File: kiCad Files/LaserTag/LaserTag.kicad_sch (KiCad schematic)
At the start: 9 parts, among them J1 Conn_01x01_Male, J2 Conn_01x02_Male, U1 LM741

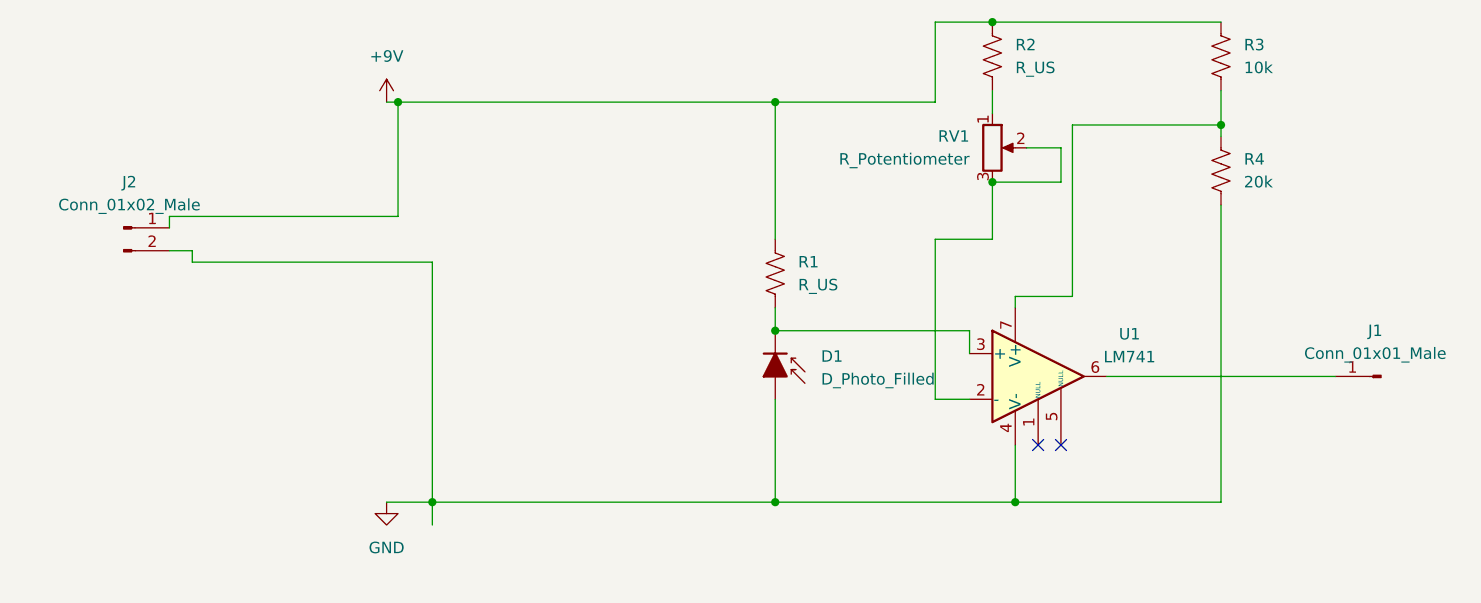
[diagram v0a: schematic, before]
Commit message: transmitter Circuit created + receiver resized
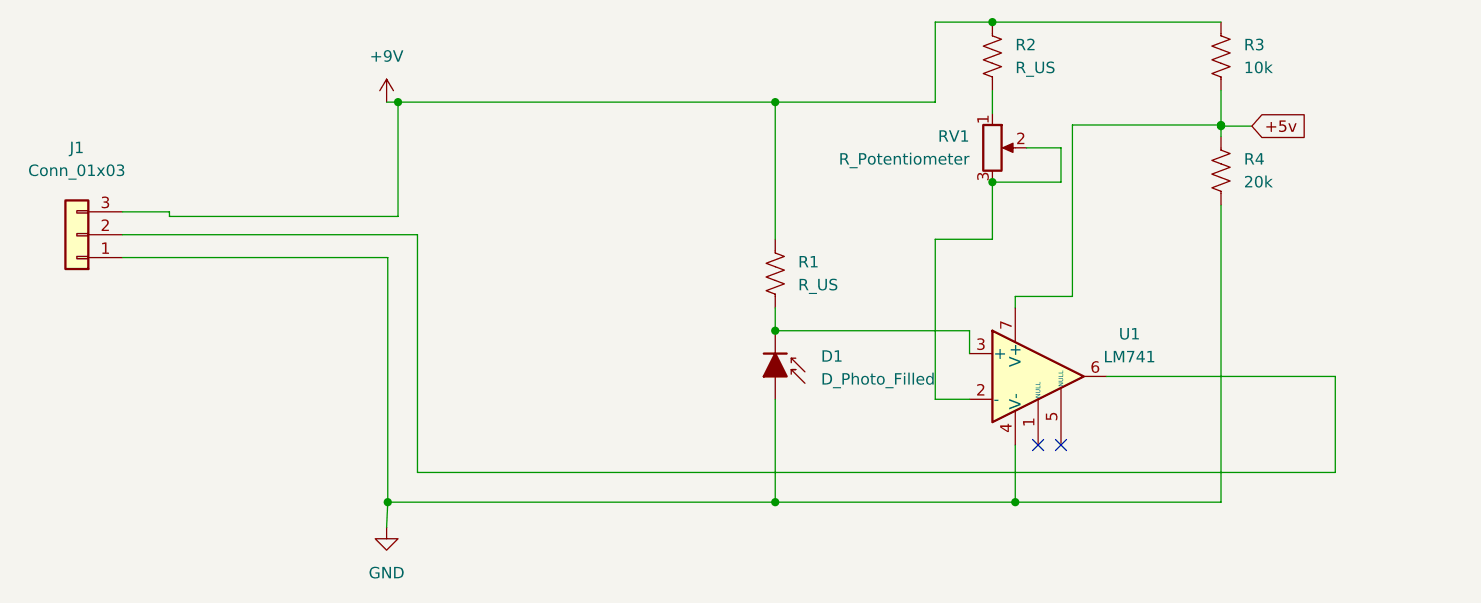
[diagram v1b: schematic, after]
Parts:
- removed J1: Conn_01x01_Male, Connector_PinHeader_1.00mm:PinHeader_1x01_P1.00mm_Vertical, symbol Connector:Conn_01x01_Male
- removed J2: Conn_01x02_Male, Connector_PinHeader_2.00mm:PinHeader_1x02_P2.00mm_Vertical, symbol Connector:Conn_01x02_Male
- added J1: Conn_01x03, symbol Connector_Generic:Conn_01x03
- D1: footprint (none) -> OptoDevice:R_LDR_4.9x4.2mm_P2.54mm_Vertical
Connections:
- net +9V: now also J1.3 (Pin_3)
- net GND: now also J1.1 (Pin_1)
- net +5v: now reaches R3.2, R4.1, U1.7 (V+)
- net at U1.6: now also J1.2 (Pin_2)
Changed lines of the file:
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@@
   (junction (at 118.11 66.04) (diameter 0) (color 0 0 0 0)
   )
+  (junction (at 167.64 68.707) (diameter 0) (color 0 0 0 0)
+  )
   (junction (at 76.2 66.04) (diameter 0) (color 0 0 0 0)
   )
   (junction (at 118.11 91.44) (diameter 0) (color 0 0 0 0)
   )
-  (junction (at 80.01 110.49) (diameter 0) (color 0 0 0 0)
-  )
   (junction (at 142.24 74.93) (diameter 0) (color 0 0 0 0)
+  )
+  (junction (at 75.057 110.49) (diameter 0) (color 0 0 0 0)
   )
   (junction (at 118.11 110.49) (diameter 0) (color 0 0 0 0)
@@
   (no_connect (at 149.86 104.14))
   (no_connect (at 147.32 104.14))
+  (wire (pts (xy 78.359 107.188) (xy 78.359 80.772))
+    (stroke (width 0) (type default) (color 0 0 0 0))
+  )
   (wire (pts (xy 118.11 88.9) (xy 118.11 91.44))
     (stroke (width 0) (type default) (color 0 0 0 0))
@@
     (stroke (width 0) (type default) (color 0 0 0 0))
   )
+  (wire (pts (xy 50.8 78.232) (xy 50.8 78.74))
+    (stroke (width 0) (type default) (color 0 0 0 0))
+  )
   (wire (pts (xy 76.2 66.04) (xy 118.11 66.04))
     (stroke (width 0) (type default) (color 0 0 0 0))
@@
     (stroke (width 0) (type default) (color 0 0 0 0))
   )
-  (wire (pts (xy 53.34 83.82) (xy 80.01 83.82))
-    (stroke (width 0) (type default) (color 0 0 0 0))
-  )
   (wire (pts (xy 118.11 66.04) (xy 118.11 81.28))
     (stroke (width 0) (type default) (color 0 0 0 0))
   )
+  (wire (pts (xy 45.593 83.312) (xy 75.057 83.312))
+    (stroke (width 0) (type default) (color 0 0 0 0))
+  )
   (wire (pts (xy 76.2 66.04) (xy 76.2 78.74))
     (stroke (width 0) (type default) (color 0 0 0 0))
@@
     (stroke (width 0) (type default) (color 0 0 0 0))
   )
-  (wire (pts (xy 53.34 83.82) (xy 53.34 82.55))
-    (stroke (width 0) (type default) (color 0 0 0 0))
-  )
   (wire (pts (xy 151.13 68.58) (xy 151.13 87.63))
     (stroke (width 0) (type default) (color 0 0 0 0))
@@
     (stroke (width 0) (type default) (color 0 0 0 0))
   )
-  (wire (pts (xy 80.01 83.82) (xy 80.01 110.49))
+  (wire (pts (xy 167.64 68.707) (xy 167.64 69.85))
     (stroke (width 0) (type default) (color 0 0 0 0))
   )
@@
     (stroke (width 0) (type default) (color 0 0 0 0))
   )
-  (wire (pts (xy 118.11 110.49) (xy 80.01 110.49))
+  (wire (pts (xy 74.93 113.284) (xy 75.057 110.49))
     (stroke (width 0) (type default) (color 0 0 0 0))
   )
@@
     (stroke (width 0) (type default) (color 0 0 0 0))
   )
+  (wire (pts (xy 180.34 96.52) (xy 180.34 107.188))
+    (stroke (width 0) (type default) (color 0 0 0 0))
+  )
   (wire (pts (xy 154.94 96.52) (xy 180.34 96.52))
     (stroke (width 0) (type default) (color 0 0 0 0))
@@
     (stroke (width 0) (type default) (color 0 0 0 0))
   )
+  (wire (pts (xy 180.34 107.188) (xy 78.359 107.188))
+    (stroke (width 0) (type default) (color 0 0 0 0))
+  )
+  (wire (pts (xy 75.057 110.49) (xy 118.11 110.49))
+    (stroke (width 0) (type default) (color 0 0 0 0))
+  )
+  (wire (pts (xy 45.593 78.232) (xy 50.8 78.232))
+    (stroke (width 0) (type default) (color 0 0 0 0))
+  )
   (wire (pts (xy 167.64 64.77) (xy 167.64 68.58))
     (stroke (width 0) (type default) (color 0 0 0 0))
   )
-  (wire (pts (xy 167.64 68.58) (xy 167.64 69.85))
-    (stroke (width 0) (type default) (color 0 0 0 0))
-  )
-  (wire (pts (xy 80.01 110.49) (xy 74.93 110.49))
+  (wire (pts (xy 167.64 68.58) (xy 167.64 68.707))
+    (stroke (width 0) (type default) (color 0 0 0 0))
+  )
+  (wire (pts (xy 75.057 83.312) (xy 75.057 110.49))
     (stroke (width 0) (type default) (color 0 0 0 0))
   )
@@
     (stroke (width 0) (type default) (color 0 0 0 0))
   )
+  (wire (pts (xy 167.64 68.707) (xy 171.069 68.707))
+    (stroke (width 0) (type default) (color 0 0 0 0))
+  )
+  (wire (pts (xy 45.593 80.772) (xy 78.359 80.772))
+    (stroke (width 0) (type default) (color 0 0 0 0))
+  )
   (wire (pts (xy 142.24 74.93) (xy 142.24 81.28))
     (stroke (width 0) (type default) (color 0 0 0 0))
   )
-  (wire (pts (xy 50.8 82.55) (xy 53.34 82.55))
-    (stroke (width 0) (type default) (color 0 0 0 0))
-  )
   (wire (pts (xy 135.89 57.15) (xy 142.24 57.15))
     (stroke (width 0) (type default) (color 0 0 0 0))
@@
     (stroke (width 0) (type default) (color 0 0 0 0))
   )
-  (wire (pts (xy 50.8 78.74) (xy 50.8 80.01))
-    (stroke (width 0) (type default) (color 0 0 0 0))
-  )
-  (wire (pts (xy 80.01 110.49) (xy 80.01 113.03))
-    (stroke (width 0) (type default) (color 0 0 0 0))
-  )
   (wire (pts (xy 135.89 81.28) (xy 135.89 99.06))
     (stroke (width 0) (type default) (color 0 0 0 0))
@@
   (wire (pts (xy 135.89 66.04) (xy 135.89 57.15))
     (stroke (width 0) (type default) (color 0 0 0 0))
+  )
+  (global_label "+5v" (shape input) (at 171.069 68.707 0) (fields_autoplaced)
+    (effects (font (size 1.27 1.27)) (justify left))
+    (property "Intersheet References" "${INTERSHEET_REFS}" (id 0) (at 177.2316 68.6276 0)
+      (effects (font (size 1.27 1.27)) (justify left) hide)
+    )
   )
   (symbol (lib_id "Device:R_Potentiometer") (at 142.24 71.12 0) (unit 1)
@@
     (pin "3")
   )
-  (symbol (lib_id "power:GND") (at 74.93 110.49 0) (unit 1)
-    (in_bom yes) (on_board yes) (fields_autoplaced)
-    (property "Reference" "#PWR0102" (id 0) (at 74.93 116.84 0)
-      (effects (font (size 1.27 1.27)) hide)
-    )
-    (property "Value" "GND" (id 1) (at 74.93 115.57 0))
-    (property "Footprint" "" (id 2) (at 74.93 110.49 0)
-      (effects (font (size 1.27 1.27)) hide)
-    )
-    (property "Datasheet" "" (id 3) (at 74.93 110.49 0)
+  (symbol (lib_id "power:GND") (at 74.93 113.284 0) (unit 1)
+    (in_bom yes) (on_board yes) (fields_autoplaced)
+    (property "Reference" "#PWR0102" (id 0) (at 74.93 119.634 0)
+      (effects (font (size 1.27 1.27)) hide)
+    )
+    (property "Value" "GND" (id 1) (at 74.93 118.364 0))
+    (property "Footprint" "" (id 2) (at 74.93 113.284 0)
+      (effects (font (size 1.27 1.27)) hide)
+    )
+    (property "Datasheet" "" (id 3) (at 74.93 113.284 0)
       (effects (font (size 1.27 1.27)) hide)
     )
@@
     (pin "8")
   )
+  (symbol (lib_id "Connector_Generic:Conn_01x03") (at 40.513 80.772 180) (unit 1)
+    (in_bom yes) (on_board yes) (fields_autoplaced)
+    (property "Reference" "J1" (id 0) (at 40.513 71.12 0))
+    (property "Value" "Conn_01x03" (id 1) (at 40.513 73.66 0))
+    (property "Footprint" "" (id 2) (at 40.513 80.772 0)
+      (effects (font (size 1.27 1.27)) hide)
+    )
+    (property "Datasheet" "~" (id 3) (at 40.513 80.772 0)
+      (effects (font (size 1.27 1.27)) hide)
+    )
+    (pin "1")
+    (pin "2")
+    (pin "3")
+  )
   (symbol (lib_id "Device:R_US") (at 118.11 85.09 0) (unit 1)
     (in_bom yes) (on_board yes) (fields_autoplaced)
@@
     (pin "2")
   )
-  (symbol (lib_id "Connector:Conn_01x02_Male") (at 45.72 80.01 0) (unit 1)
-    (in_bom yes) (on_board yes) (fields_autoplaced)
-    (property "Reference" "J2" (id 0) (at 46.355 74.93 0))
-    (property "Value" "Conn_01x02_Male" (id 1) (at 46.355 77.47 0))
-    (property "Footprint" "Connector_PinHeader_2.00mm:PinHeader_1x02_P2.00mm_Vertical" (id 2) (at 45.72 80.01 0)
-      (effects (font (size 1.27 1.27)) hide)
-    )
-    (property "Datasheet" "~" (id 3) (at 45.72 80.01 0)
-      (effects (font (size 1.27 1.27)) hide)
-    )
-    (pin "1")
-    (pin "2")
-  )
   (symbol (lib_id "Device:R_US") (at 167.64 60.96 0) (unit 1)
     (in_bom yes) (on_board yes) (fields_autoplaced)
@@
       (effects (font (size 1.27 1.27)) (justify left))
     )
-    (property "Footprint" "" (id 2) (at 118.11 95.25 0)
+    (property "Footprint" "OptoDevice:R_LDR_4.9x4.2mm_P2.54mm_Vertical" (id 2) (at 118.11 95.25 0)
       (effects (font (size 1.27 1.27)) hide)
     )
@@
     (pin "1")
     (pin "2")
-  )
-  (symbol (lib_id "Connector:Conn_01x01_Male") (at 185.42 96.52 180) (unit 1)
-    (in_bom yes) (on_board yes) (fields_autoplaced)
-    (property "Reference" "J1" (id 0) (at 184.785 91.44 0))
-    (property "Value" "Conn_01x01_Male" (id 1) (at 184.785 93.98 0))
-    (property "Footprint" "Connector_PinHeader_1.00mm:PinHeader_1x01_P1.00mm_Vertical" (id 2) (at 185.42 96.52 0)
-      (effects (font (size 1.27 1.27)) hide)
-    )
-    (property "Datasheet" "~" (id 3) (at 185.42 96.52 0)
-      (effects (font (size 1.27 1.27)) hide)
-    )
-    (pin "1")
   )
   (sheet_instances
@@
       (reference "D1") (unit 1) (value "D_Photo_Filled") (footprint "OptoDevice:R_LDR_4.9x4.2mm_P2.54mm_Vertical")
     )
-    (path "/b1213d25-105e-455b-83df-a5c924a8d0cc"
-      (reference "J1") (unit 1) (value "Conn_01x01_Male") (footprint "Connector_PinHeader_1.00mm:PinHeader_1x01_P1.00mm_Vertical")
-    )
-    (path "/5cc52a57-e83e-4f18-af2c-d45b63357cac"
-      (reference "J2") (unit 1) (value "Conn_01x02_Male") (footprint "Connector_PinHeader_2.00mm:PinHeader_1x02_P2.00mm_Vertical")
+    (path "/42d27032-5c46-4dc2-b11b-f95c4eced5df"
+      (reference "J1") (unit 1) (value "Conn_01x03") (footprint "Connector_PinHeader_1.00mm:PinHeader_1x03_P1.00mm_Vertical")
     )
     (path "/55b26018-64d5-4f72-aef8-3c5d6628eb47"

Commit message: creds to schematic
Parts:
- J1: footprint (none) -> Connector_PinHeader_1.00mm:PinHeader_1x03_P1.00mm_Vertical
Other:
- note added: "By Rosnel Leyva-Cortes"
- note added: "Receiver Circuit"
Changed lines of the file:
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@@
     (stroke (width 0) (type default) (color 0 0 0 0))
+  )
+  (text "Receiver Circuit\n" (at 186.563 190.246 0)
+    (effects (font (size 1.27 1.27)) (justify left bottom))
+  )
+  (text "By Rosnel Leyva-Cortes\n" (at 207.645 186.944 0)
+    (effects (font (size 1.27 1.27)) (justify left bottom))
   )
   (global_label "+5v" (shape input) (at 171.069 68.707 0) (fields_autoplaced)
@@
     (property "Reference" "J1" (id 0) (at 40.513 71.12 0))
     (property "Value" "Conn_01x03" (id 1) (at 40.513 73.66 0))
-    (property "Footprint" "" (id 2) (at 40.513 80.772 0)
+    (property "Footprint" "Connector_PinHeader_1.00mm:PinHeader_1x03_P1.00mm_Vertical" (id 2) (at 40.513 80.772 0)
       (effects (font (size 1.27 1.27)) hide)
     )
